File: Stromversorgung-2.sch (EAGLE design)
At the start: 16 parts, among them J1 DCJ0202, U1 TSR 2-2450, U2 TSR 1-2433, U3 TSR 2-2450, X1 Ein/Aus, X2 MAC64L

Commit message: Layouts angepasst
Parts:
- R1, R2, R3, R4: device rcl:R-EU_0204/5 -> rcl:R-EU_R1206
- U1, U3: value TSR 2-2450 -> TSR2-2450; device _traco_tsr-1:TSR_1-2450 -> TSR:TSR2-2450
- U2: value TSR 1-2433 -> TSR1-2433; device _traco_tsr-1:TSR_1-2433 -> TSR:TSR1-2433
- X1: device con-phoenix-508:MSTBV2 -> con-phoenix-508:MSTBA2
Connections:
- net +24V: now also X1-2.1; no longer X1-1.1
- net GND: now also X2.A11, X2.A13, X2.A27, X2.C13
- net N$1: now also X1-1.1; no longer X1-2.1
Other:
- moved on the sheet: X1-1, X1-2
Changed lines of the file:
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@@
 <class number="0" name="default" width="0" drill="0">
 </class>
-<class number="1" name="24V" width="0.8128" drill="0">
+<class number="1" name="24V" width="0" drill="0">
 <clearance class="1" value="0.4064"/>
 </class>
 </classes>
 <parts>
-<part name="X1" library="con-phoenix-508" deviceset="MSTBV2" device="" value="Ein/Aus"/>
+<part name="X1" library="con-phoenix-508" deviceset="MSTBA2" device="" value="Ein/Aus"/>
 <part name="LED1" library="led" deviceset="LED" device="3MM" value="2mA ge"/>
 <part name="LED2" library="led" deviceset="LED" device="3MM" value="2mA ge"/>
 <part name="LED3" library="led" deviceset="LED" device="3MM" value="2mA ge"/>
-<part name="R1" library="rcl" deviceset="R-EU_" device="0204/5" value="1k5"/>
-<part name="R2" library="rcl" deviceset="R-EU_" device="0204/5" value="560"/>
-<part name="R3" library="rcl" deviceset="R-EU_" device="0204/5" value="1k5"/>
-<part name="U1" library="_traco_tsr-1" deviceset="TSR_1-*" device="" technology="2450" value="TSR 2-2450"/>
-<part name="U2" library="_traco_tsr-1" deviceset="TSR_1-*" device="" technology="2433" value="TSR 1-2433"/>
-<part name="U3" library="_traco_tsr-1" deviceset="TSR_1-*" device="" technology="2450" value="TSR 2-2450"/>
+<part name="R1" library="rcl" deviceset="R-EU_" device="R1206" value="1k5"/>
+<part name="R2" library="rcl" deviceset="R-EU_" device="R1206" value="560"/>
+<part name="R3" library="rcl" deviceset="R-EU_" device="R1206" value="1k5"/>
+<part name="U1" library="TSR" deviceset="TSR2-*" device="" technology="2450" value="TSR2-2450"/>
+<part name="U2" library="TSR" deviceset="TSR1-*" device="" technology="2433" value="TSR1-2433"/>
+<part name="U3" library="TSR" deviceset="TSR2-*" device="" technology="2450" value="TSR2-2450"/>
 <part name="FRAME1" library="frames" deviceset="A4L-LOC" device=""/>
 <part name="GND1" library="supply1" deviceset="GND" device=""/>
@@
 <part name="C1" library="rcl" deviceset="CPOL-EU" device="E2-5" value="22µF 50V Low-ESR"/>
 <part name="C2" library="rcl" deviceset="CPOL-EU" device="E2-5" value="22µF 50V Low-ESR"/>
-<part name="R4" library="rcl" deviceset="R-EU_" device="0204/5" value="12k"/>
+<part name="R4" library="rcl" deviceset="R-EU_" device="R1206" value="12k"/>
 <part name="LED4" library="led" deviceset="LED" device="3MM" value="2mA ge"/>
 </parts>
@@
 </plain>
 <instances>
-<instance part="X1" gate="-1" x="139.7" y="7.62" rot="R180"/>
-<instance part="X1" gate="-2" x="139.7" y="12.7" rot="R180"/>
+<instance part="X1" gate="-1" x="132.08" y="12.7" rot="R180"/>
+<instance part="X1" gate="-2" x="132.08" y="17.78" rot="R180"/>
 <instance part="LED1" gate="G$1" x="185.42" y="40.64"/>
 <instance part="LED2" gate="G$1" x="205.74" y="40.64"/>
@@
 <instance part="R2" gate="G$1" x="205.74" y="50.8" rot="R90"/>
 <instance part="R3" gate="G$1" x="226.06" y="50.8" rot="R90"/>
-<instance part="U1" gate="G$1" x="40.64" y="152.4"/>
-<instance part="U2" gate="G$1" x="124.46" y="152.4"/>
-<instance part="U3" gate="G$1" x="213.36" y="152.4"/>
+<instance part="U1" gate="U1" x="40.64" y="152.4"/>
+<instance part="U2" gate="U1" x="124.46" y="152.4"/>
+<instance part="U3" gate="U1" x="213.36" y="152.4"/>
 <instance part="FRAME1" gate="G$1" x="-5.08" y="-5.08"/>
 <instance part="GND1" gate="1" x="15.24" y="111.76"/>
@@
 </segment>
 <segment>
-<pinref part="U1" gate="G$1" pin="VO"/>
+<pinref part="U1" gate="U1" pin="VO"/>
 <wire x1="50.8" y1="152.4" x2="55.88" y2="152.4" width="0.1524" layer="91"/>
 <label x="55.88" y="152.4" size="1.778" layer="95" xref="yes"/>
@@
 </segment>
 <segment>
-<pinref part="U3" gate="G$1" pin="VO"/>
+<pinref part="U3" gate="U1" pin="VO"/>
 <wire x1="223.52" y1="152.4" x2="228.6" y2="152.4" width="0.1524" layer="91"/>
 <label x="228.6" y="152.4" size="1.778" layer="95" xref="yes"/>
@@
 <segment>
 <label x="139.7" y="152.4" size="1.778" layer="95" xref="yes"/>
-<pinref part="U2" gate="G$1" pin="VO"/>
+<pinref part="U2" gate="U1" pin="VO"/>
 <wire x1="134.62" y1="152.4" x2="139.7" y2="152.4" width="0.1524" layer="91"/>
 </segment>
@@
 <net name="+24V" class="1">
 <segment>
-<pinref part="U1" gate="G$1" pin="VI"/>
+<pinref part="U1" gate="U1" pin="VI"/>
 <wire x1="30.48" y1="152.4" x2="17.78" y2="152.4" width="0.1524" layer="91"/>
 <label x="10.16" y="152.4" size="1.778" layer="95" rot="R180" xref="yes"/>
@@
 </segment>
 <segment>
-<pinref part="U3" gate="G$1" pin="VI"/>
+<pinref part="U3" gate="U1" pin="VI"/>
 <wire x1="203.2" y1="152.4" x2="190.5" y2="152.4" width="0.1524" layer="91"/>
 <label x="182.88" y="152.4" size="1.778" layer="95" rot="R180" xref="yes"/>
@@
 </segment>
 <segment>
-<pinref part="X1" gate="-1" pin="1"/>
-<wire x1="134.62" y1="7.62" x2="132.08" y2="7.62" width="0.1524" layer="91"/>
-<label x="132.08" y="7.62" size="1.778" layer="95" rot="MR0"/>
-</segment>
-<segment>
 <pinref part="R4" gate="G$1" pin="2"/>
 <wire x1="243.84" y1="55.88" x2="243.84" y2="60.96" width="0.1524" layer="91"/>
@@
 </segment>
 <segment>
-<pinref part="U2" gate="G$1" pin="VI"/>
+<pinref part="U2" gate="U1" pin="VI"/>
 <wire x1="109.22" y1="152.4" x2="114.3" y2="152.4" width="0.1524" layer="91"/>
 <label x="109.22" y="152.4" size="1.778" layer="95" rot="R180" xref="yes"/>
+</segment>
+<segment>
+<pinref part="X1" gate="-2" pin="1"/>
+<wire x1="127" y1="17.78" x2="119.38" y2="17.78" width="0.1524" layer="91"/>
+<label x="119.38" y="17.78" size="1.778" layer="95" rot="MR0"/>
 </segment>
 </net>
@@
 </segment>
 <segment>
-<pinref part="U1" gate="G$1" pin="GND"/>
+<pinref part="U1" gate="U1" pin="GND"/>
 <wire x1="40.64" y1="144.78" x2="40.64" y2="139.7" width="0.1524" layer="91"/>
 <label x="40.64" y="137.16" size="1.778" layer="95" rot="R270" xref="yes"/>
@@
 </segment>
 <segment>
-<pinref part="U2" gate="G$1" pin="GND"/>
+<pinref part="U2" gate="U1" pin="GND"/>
 <wire x1="124.46" y1="144.78" x2="124.46" y2="137.16" width="0.1524" layer="91"/>
 <label x="124.46" y="137.16" size="1.778" layer="95" rot="R270" xref="yes"/>
 </segment>
 <segment>
-<pinref part="U3" gate="G$1" pin="GND"/>
+<pinref part="U3" gate="U1" pin="GND"/>
 <wire x1="213.36" y1="144.78" x2="213.36" y2="139.7" width="0.1524" layer="91"/>
 <label x="213.36" y="137.16" size="1.778" layer="95" rot="R270" xref="yes"/>
@@
 <label x="58.42" y="15.24" size="1.778" layer="95"/>
 </segment>
-</net>
-<net name="N$1" class="1">
-<segment>
-<pinref part="J1" gate="G$1" pin="1"/>
-<pinref part="X1" gate="-2" pin="1"/>
-<wire x1="106.68" y1="12.7" x2="134.62" y2="12.7" width="0.1524" layer="91"/>
+<segment>
+<pinref part="X2" gate="G$1" pin="A11"/>
+<wire x1="38.1" y1="63.5" x2="33.02" y2="63.5" width="0.1524" layer="91"/>
+<label x="33.02" y="63.5" size="1.778" layer="95" rot="MR0"/>
+</segment>
+<segment>
+<pinref part="X2" gate="G$1" pin="A13"/>
+<wire x1="38.1" y1="58.42" x2="33.02" y2="58.42" width="0.1524" layer="91"/>
+<label x="33.02" y="58.42" size="1.778" layer="95" rot="MR0"/>
+</segment>
+<segment>
+<pinref part="X2" gate="G$1" pin="C13"/>
+<wire x1="53.34" y1="58.42" x2="58.42" y2="58.42" width="0.1524" layer="91"/>
+<label x="58.42" y="58.42" size="1.778" layer="95"/>
+</segment>
+<segment>
+<pinref part="X2" gate="G$1" pin="A27"/>
+<wire x1="38.1" y1="22.86" x2="33.02" y2="22.86" width="0.1524" layer="91"/>
+<label x="33.02" y="22.86" size="1.778" layer="95" rot="MR0"/>
 </segment>
 </net>
@@
 </segment>
 </net>
+<net name="N$1" class="0">
+<segment>
+<pinref part="J1" gate="G$1" pin="1"/>
+<pinref part="X1" gate="-1" pin="1"/>
+<wire x1="106.68" y1="12.7" x2="127" y2="12.7" width="0.1524" layer="91"/>
+</segment>
+</net>

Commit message: Layouts angepasst
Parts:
- removed J1: DCJ0202, con-jack:DCJ0202
- added X3: Ein/Aus, con-phoenix-508:MSTBA2
- U3: value TSR2-2450 -> TSR1-2425; device TSR:TSR2-2450 -> TSR:TSR1-2425
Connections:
- removed net N$1: J1.1, X1-1.1
- new net +24V_IN: X1-1.1, X3-2.1
- net GND: now also X3-1.1; no longer J1.3
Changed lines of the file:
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@@
 <part name="U1" library="TSR" deviceset="TSR2-*" device="" technology="2450" value="TSR2-2450"/>
 <part name="U2" library="TSR" deviceset="TSR1-*" device="" technology="2433" value="TSR1-2433"/>
-<part name="U3" library="TSR" deviceset="TSR2-*" device="" technology="2450" value="TSR2-2450"/>
+<part name="U3" library="TSR" deviceset="TSR1-*" device="" technology="2425" value="TSR1-2425"/>
 <part name="FRAME1" library="frames" deviceset="A4L-LOC" device=""/>
 <part name="GND1" library="supply1" deviceset="GND" device=""/>
-<part name="J1" library="con-jack" deviceset="DCJ0202" device=""/>
 <part name="X2" library="con-vg" deviceset="MAC64L" device=""/>
 <part name="C1" library="rcl" deviceset="CPOL-EU" device="E2-5" value="22µF 50V Low-ESR"/>
@@
 <part name="R4" library="rcl" deviceset="R-EU_" device="R1206" value="12k"/>
 <part name="LED4" library="led" deviceset="LED" device="3MM" value="2mA ge"/>
+<part name="X3" library="con-phoenix-508" deviceset="MSTBA2" device="" value="Ein/Aus"/>
 </parts>
 <sheets>
@@
 <instance part="FRAME1" gate="G$1" x="-5.08" y="-5.08"/>
 <instance part="GND1" gate="1" x="15.24" y="111.76"/>
-<instance part="J1" gate="G$1" x="99.06" y="10.16"/>
 <instance part="X2" gate="G$1" x="45.72" y="50.8"/>
 <instance part="C1" gate="G$1" x="17.78" y="147.32"/>
@@
 <instance part="R4" gate="G$1" x="243.84" y="50.8" rot="R90"/>
 <instance part="LED4" gate="G$1" x="243.84" y="40.64"/>
+<instance part="X3" gate="-1" x="132.08" y="40.64" rot="R180"/>
+<instance part="X3" gate="-2" x="132.08" y="45.72" rot="R180"/>
 </instances>
 <busses>
@@
 </segment>
 <segment>
-<pinref part="J1" gate="G$1" pin="3"/>
-<wire x1="106.68" y1="7.62" x2="111.76" y2="7.62" width="0.1524" layer="91"/>
-<label x="111.76" y="7.62" size="1.778" layer="95"/>
-</segment>
-<segment>
 <pinref part="X2" gate="G$1" pin="A29"/>
 <wire x1="38.1" y1="17.78" x2="33.02" y2="17.78" width="0.1524" layer="91"/>
@@
 <label x="33.02" y="22.86" size="1.778" layer="95" rot="MR0"/>
 </segment>
+<segment>
+<pinref part="X3" gate="-1" pin="1"/>
+<wire x1="127" y1="40.64" x2="119.38" y2="40.64" width="0.1524" layer="91"/>
+<label x="119.38" y="40.64" size="1.778" layer="95" rot="MR0"/>
+</segment>
 </net>
 <net name="N$3" class="0">
@@
 </segment>
 </net>
-<net name="N$1" class="0">
-<segment>
-<pinref part="J1" gate="G$1" pin="1"/>
+<net name="+24V_IN" class="0">
+<segment>
+<pinref part="X3" gate="-2" pin="1"/>
+<wire x1="127" y1="45.72" x2="119.38" y2="45.72" width="0.1524" layer="91"/>
+<label x="119.38" y="45.72" size="1.778" layer="95" rot="MR0"/>
+</segment>
+<segment>
 <pinref part="X1" gate="-1" pin="1"/>
-<wire x1="106.68" y1="12.7" x2="127" y2="12.7" width="0.1524" layer="91"/>
-</segment>
-</net>
+<wire x1="119.38" y1="12.7" x2="127" y2="12.7" width="0.1524" layer="91"/>
+<label x="119.38" y="12.7" size="1.778" layer="95" rot="MR0"/>
+</segment>
+</net>

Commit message: Layouts angepasst
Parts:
- added D1: MBRS 540T3G, diode:SCHOTTKY-DIODESMC
- added F1: 30V / 2,5A, fuse:LITTLEFUSE
- X3: value Ein/Aus -> Eingang
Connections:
- new net +24V_IN_RAW: F1.2, X3-2.1
- net +24V: now also D1.C
- net +24V_IN: now also F1.1; no longer X3-2.1
- net GND: now also D1.A
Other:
- moved on the sheet: X1-1, X1-2, X3-1, X3-2
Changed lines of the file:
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@@
 <part name="R4" library="rcl" deviceset="R-EU_" device="R1206" value="12k"/>
 <part name="LED4" library="led" deviceset="LED" device="3MM" value="2mA ge"/>
-<part name="X3" library="con-phoenix-508" deviceset="MSTBA2" device="" value="Ein/Aus"/>
+<part name="X3" library="con-phoenix-508" deviceset="MSTBA2" device="" value="Eingang"/>
+<part name="D1" library="diode" deviceset="SCHOTTKY-DIODE" device="SMC" value="MBRS 540T3G"/>
+<part name="F1" library="fuse" deviceset="LITTLEFUSE" device="" value="30V / 2,5A"/>
 </parts>
 <sheets>
@@
 </plain>
 <instances>
-<instance part="X1" gate="-1" x="132.08" y="12.7" rot="R180"/>
-<instance part="X1" gate="-2" x="132.08" y="17.78" rot="R180"/>
+<instance part="X1" gate="-1" x="132.08" y="25.4" rot="R180"/>
+<instance part="X1" gate="-2" x="132.08" y="30.48" rot="R180"/>
 <instance part="LED1" gate="G$1" x="185.42" y="40.64"/>
 <instance part="LED2" gate="G$1" x="205.74" y="40.64"/>
@@
 <instance part="R4" gate="G$1" x="243.84" y="50.8" rot="R90"/>
 <instance part="LED4" gate="G$1" x="243.84" y="40.64"/>
-<instance part="X3" gate="-1" x="132.08" y="40.64" rot="R180"/>
-<instance part="X3" gate="-2" x="132.08" y="45.72" rot="R180"/>
+<instance part="X3" gate="-1" x="132.08" y="43.18" rot="R180"/>
+<instance part="X3" gate="-2" x="132.08" y="48.26" rot="R180"/>
+<instance part="D1" gate="G$1" x="111.76" y="10.16" rot="R90"/>
+<instance part="F1" gate="A" x="119.38" y="48.26"/>
 </instances>
 <busses>
@@
 <segment>
 <pinref part="X1" gate="-2" pin="1"/>
-<wire x1="127" y1="17.78" x2="119.38" y2="17.78" width="0.1524" layer="91"/>
-<label x="119.38" y="17.78" size="1.778" layer="95" rot="MR0"/>
+<wire x1="127" y1="30.48" x2="111.76" y2="30.48" width="0.1524" layer="91"/>
+<label x="109.22" y="30.48" size="1.778" layer="95" rot="MR0"/>
+<pinref part="D1" gate="G$1" pin="C"/>
+<wire x1="111.76" y1="30.48" x2="109.22" y2="30.48" width="0.1524" layer="91"/>
+<wire x1="111.76" y1="12.7" x2="111.76" y2="30.48" width="0.1524" layer="91"/>
+<junction x="111.76" y="30.48"/>
 </segment>
 </net>
@@
 </segment>
 <segment>
+<label x="111.76" y="43.18" size="1.778" layer="95" rot="MR0"/>
 <pinref part="X3" gate="-1" pin="1"/>
-<wire x1="127" y1="40.64" x2="119.38" y2="40.64" width="0.1524" layer="91"/>
-<label x="119.38" y="40.64" size="1.778" layer="95" rot="MR0"/>
+<wire x1="111.76" y1="43.18" x2="127" y2="43.18" width="0.1524" layer="91"/>
+</segment>
+<segment>
+<pinref part="D1" gate="G$1" pin="A"/>
+<wire x1="111.76" y1="7.62" x2="111.76" y2="5.08" width="0.1524" layer="91"/>
+<label x="111.76" y="5.08" size="1.778" layer="95"/>
 </segment>
 </net>
@@
 <net name="+24V_IN" class="0">
 <segment>
+<pinref part="X1" gate="-1" pin="1"/>
+<label x="124.46" y="25.4" size="1.778" layer="95" rot="MR0"/>
+<wire x1="124.46" y1="25.4" x2="127" y2="25.4" width="0.1524" layer="91"/>
+</segment>
+<segment>
+<pinref part="F1" gate="A" pin="1"/>
+<wire x1="111.76" y1="48.26" x2="114.3" y2="48.26" width="0.1524" layer="91"/>
+<label x="111.76" y="48.26" size="1.778" layer="95" rot="MR0"/>
+</segment>
+</net>
+<net name="+24V_IN_RAW" class="0">
+<segment>
 <pinref part="X3" gate="-2" pin="1"/>
-<wire x1="127" y1="45.72" x2="119.38" y2="45.72" width="0.1524" layer="91"/>
-<label x="119.38" y="45.72" size="1.778" layer="95" rot="MR0"/>
-</segment>
-<segment>
-<pinref part="X1" gate="-1" pin="1"/>
-<wire x1="119.38" y1="12.7" x2="127" y2="12.7" width="0.1524" layer="91"/>
-<label x="119.38" y="12.7" size="1.778" layer="95" rot="MR0"/>
-</segment>
-</net>
+<pinref part="F1" gate="A" pin="2"/>
+<wire x1="124.46" y1="48.26" x2="127" y2="48.26" width="0.1524" layer="91"/>
+</segment>
+</net>

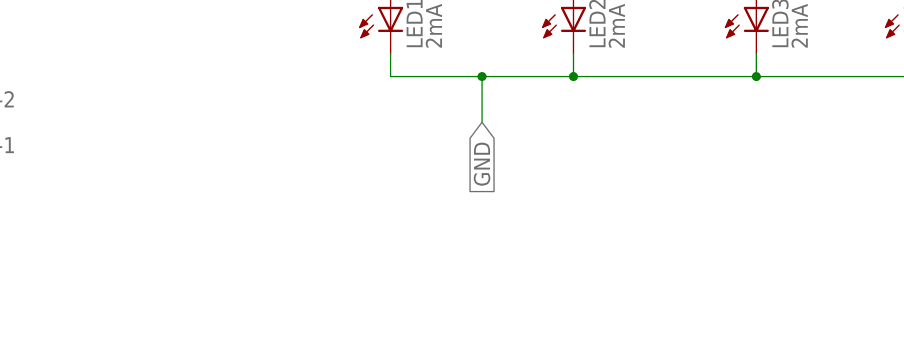
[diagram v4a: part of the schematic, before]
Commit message: Schaltpläne aufgehübscht zur Veröffentlichung
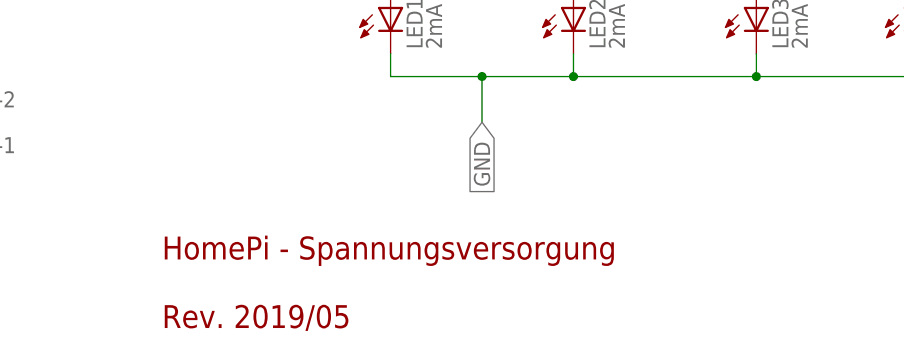
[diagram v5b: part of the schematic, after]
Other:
- note added: "HomePi - Spannungsversorgung Rev. 2019/05"
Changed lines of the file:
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@@
 <sheet>
 <plain>
+<text x="160.02" y="15.24" size="2.54" layer="94" align="top-left">HomePi - Spannungsversorgung
+Rev. 2019/05</text>
 </plain>
 <instances>
@@
 </schematic>
 </drawing>
+<compatibility>
+<note version="6.3" minversion="6.2.2" severity="warning">
+Since Version 6.2.2 text objects can contain more than one line,
+which will not be processed correctly with this version.
+</note>
+</compatibility>
 </eagle>
